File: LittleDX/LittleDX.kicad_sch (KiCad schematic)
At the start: 137 parts, among them J1 POWER, J10 PA6, J11 AudioJack2_Dual_Ground_Switch, J13 Conn_01x01, J14 Conn_01x01, J15 Conn_01x01, J16 Conn_01x01, J19 AudioJack2_Dual_Ground_Switch, J2 Barrel_Jack, J20 Conn_01x02, J22 Conn_01x02, J23 Conn_01x01, J24 TRANSMIT, J25 Conn_01x04, J26 USB_B, J27 Conn_01x04, J3 Conn_01x01, J4 Conn_01x01, J5 CONFIG, J6 Conn_01x01, J7 Conn_01x01, J8 AudioJack2_Dual_Ground_Switch, J9 PB9, P1 Mini-DIN_6pins_ver4, Q14 MMBT3904, Q4 MMBT3904, SW1 SW_Push, SW2 SW_Push, SW3 SW_Push, SW4 SW_Push, SW5 SW_Push, SW6 SW_Push, T4 Common-Mode Choke, U1 STM32F103C8Tx, U2 LM78M05_TO252, U3 LM386, U4 AMS1117-3.3, U5 LM358, U7 MicroSD_SPI_CD, Y1 8 MHz, Y2 32.768 kHz

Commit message: JLCPCB version 2
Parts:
- removed L1: 100 uH, Inductor_SMD:L_0805_2012Metric_Pad1.15x1.40mm_HandSolder, symbol LittleDX-rescue:L
- added C45: 100 nF, Capacitor_SMD:C_0805_2012Metric_Pad1.18x1.45mm_HandSolder, symbol LittleDX-rescue:C_Small
- added C48: 10 uF, Capacitor_SMD:C_0805_2012Metric_Pad1.18x1.45mm_HandSolder, symbol LittleDX-rescue:C_Small
- added D12: 1N4148, Diode_SMD:D_SOD-123, symbol LittleDX-rescue:D
- added J21: PB12, Connector_PinHeader_2.54mm:PinHeader_1x01_P2.54mm_Vertical, symbol Connector_Generic:Conn_01x01
- added R56: 47R, Resistor_SMD:R_0805_2012Metric_Pad1.20x1.40mm_HandSolder, symbol LittleDX-rescue:R
- C9: value 100 nF -> 10 uF; LCSC C49678 -> C15850
- D2: footprint Diode_SMD:D_0805_2012Metric_Pad1.15x1.40mm_HandSolder -> LED_SMD:LED_0805_2012Metric_Pad1.15x1.40mm_HandSolder
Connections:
- net +3.3V: now also C45.2, D12.1 (K), R56.2
- net GND: now also C45.1
- net MICPADDLE: now also D12.2 (A)
- net at U3.1: now also C48.1
- net at U3.8: now also C48.2
- net at C9.1, U1.9 (VDDA): now also R56.1
- net VBAT: now reaches J20.1 (Pin_1), U1.1 (VBAT)
- net at U1.25 (PB12): now also J21.1 (Pin_1)
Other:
- moved on the sheet: C43, J20, J9

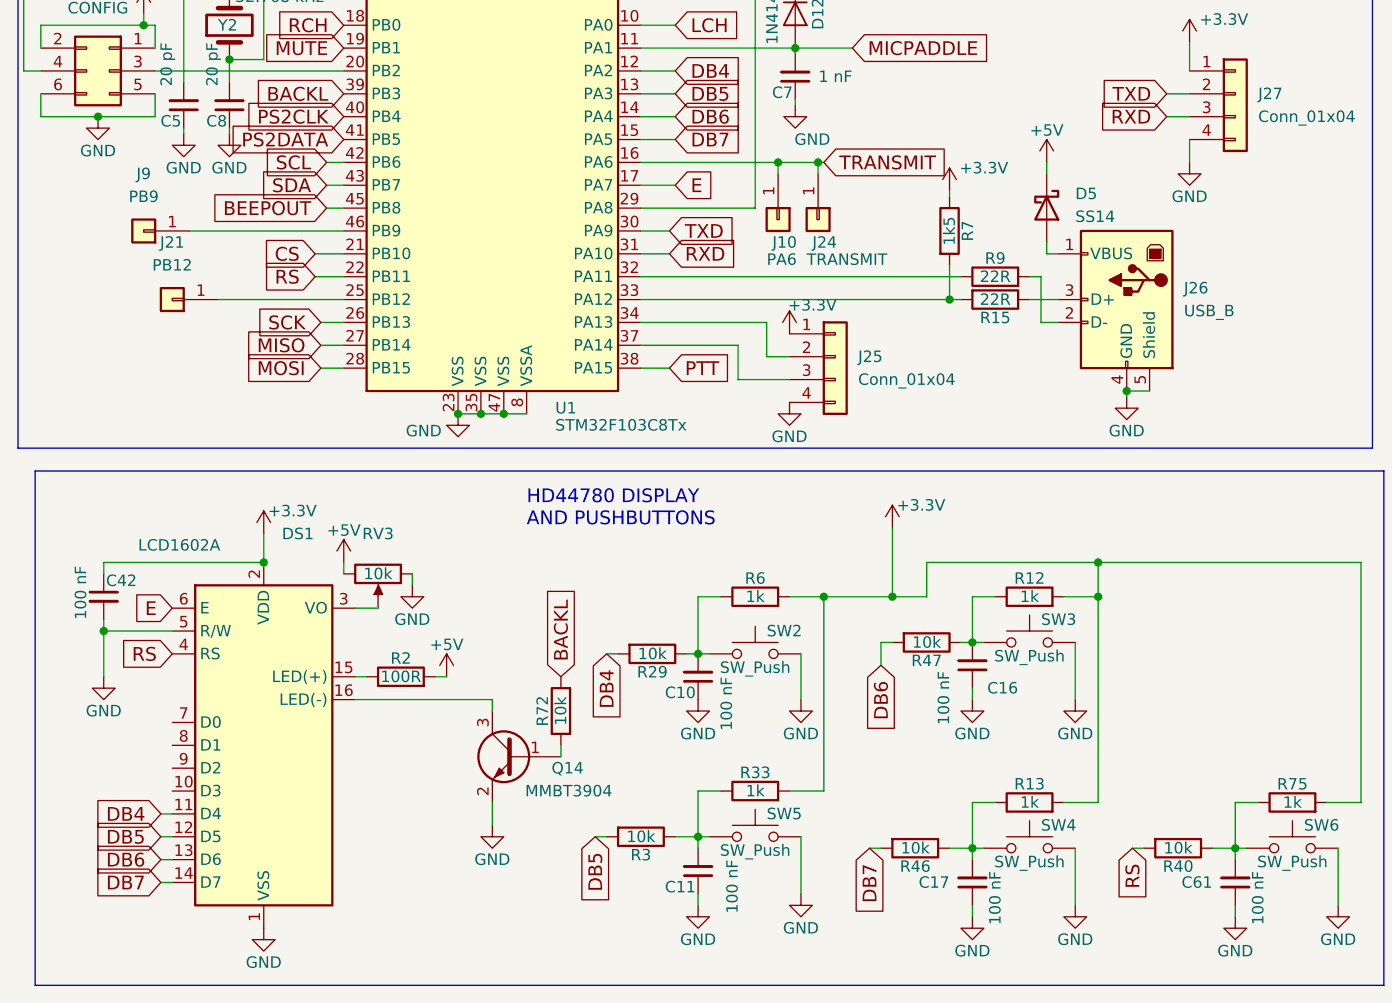
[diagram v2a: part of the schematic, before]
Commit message: Revised JLCPCB order: added negative LCD voltage supply
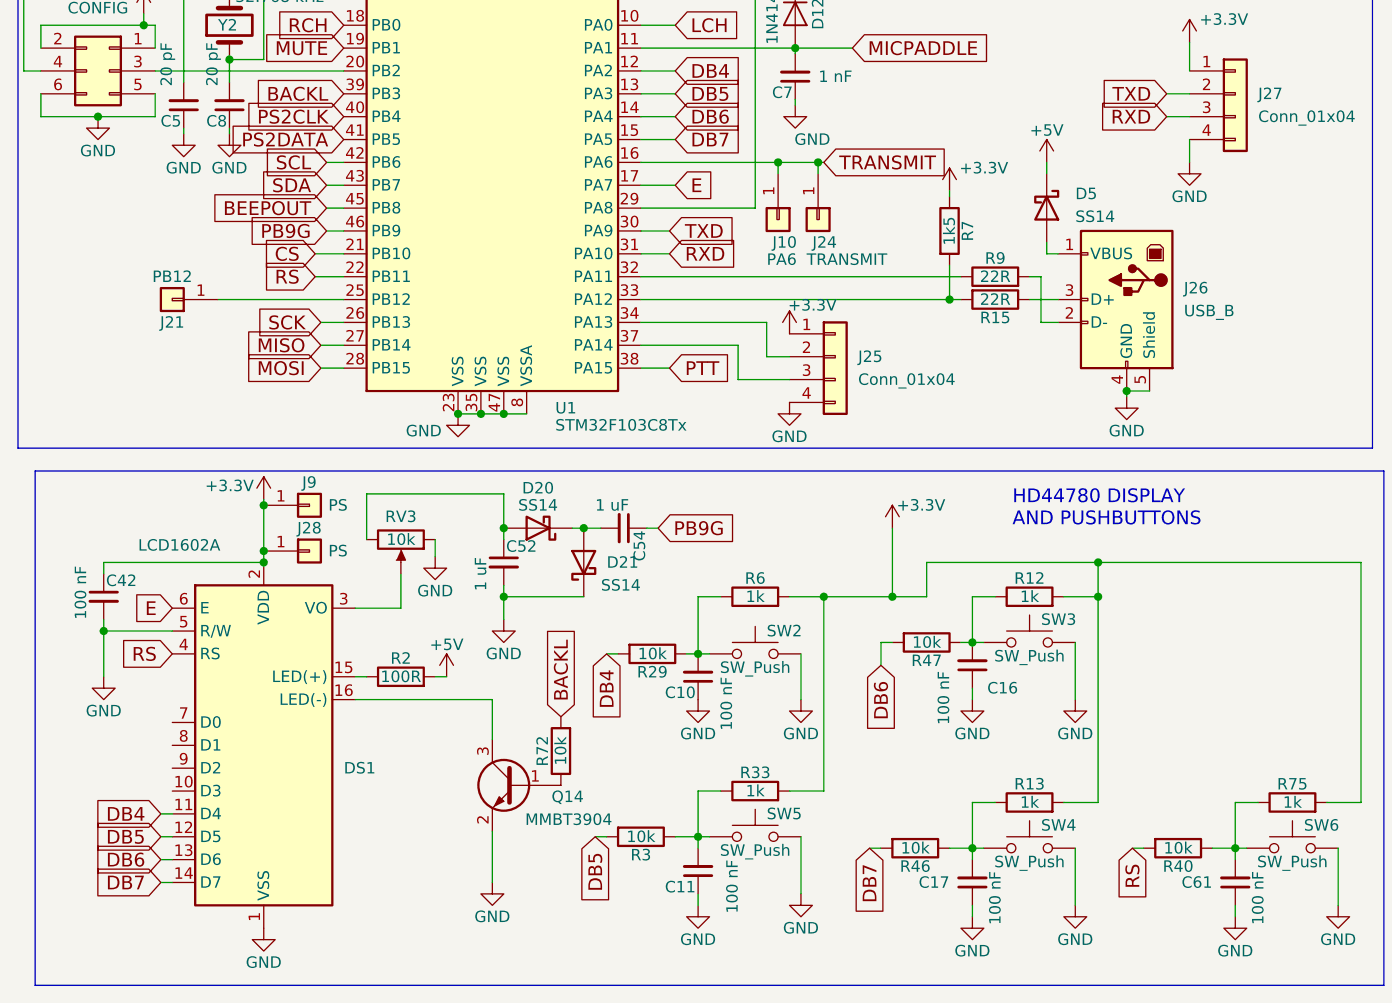
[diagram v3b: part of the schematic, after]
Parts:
- added C52, C54: 1 uF, Capacitor_SMD:C_0805_2012Metric_Pad1.18x1.45mm_HandSolder, symbol LittleDX-rescue:C_Small
- added D20, D21: SS14, Diode_SMD:D_SMA_Handsoldering, symbol Device:D_Schottky
- added J28: PS, Connector_PinHeader_2.54mm:PinHeader_1x01_P2.54mm_Vertical, symbol Connector_Generic:Conn_01x01
- J9: value PB9 -> PS
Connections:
- net +3.3V: now also J9.1 (Pin_1), J28.1 (Pin_1)
- net +5V: no longer RV3.3
- net GND: now also C52.2, D21.1 (K)
- net PB9G: now reaches U1.46 (PB9)
- net PB9G: now also C54.1; no longer J9.1 (Pin_1)
- new net: C52.1, D20.2 (A), RV3.3
- new net: C54.2, D20.1 (K), D21.2 (A)
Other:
- moved on the sheet: Q14, R72, RV3
